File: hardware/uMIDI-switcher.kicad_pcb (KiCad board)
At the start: 2 copper layers, 137.5 x 52.5 mm, 113 parts, among them Q1 BSS138, Q2 BSS138, Q3 BSS138, Q4 BSS138, Q5 BSS138, Q6 BSS138, Q7 BSS138, Q8 BSS138, U1 LM7809CT, U2 LM7809CT, U3 LM7809CT, U4 LM7809CT, X1 CONN_01X02, X10 Jack_Stacked, X11 Jack_Stacked, X14 uMIDI GPIO3, X15 LEDs, X16 uMIDI Power, X2 CONN_01X02, X3 CONN_01X02, X4 CONN_01X02, X5 Jack_Stacked, X6 Jack_Stacked, X7 Jack_Stacked, X8 Jack_Stacked, X9 Jack_Stacked

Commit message: Remove led distribution
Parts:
- removed R1, R2, R3, R4, R5, R6, R7, R8: 630, Resistors_SMD:R_0603
- removed X15: LEDs, Pin_Headers:Pin_Header_Straight_1x10
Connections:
- X14 pad 6: /Loopers and Switches/Looper4 -> (no net)

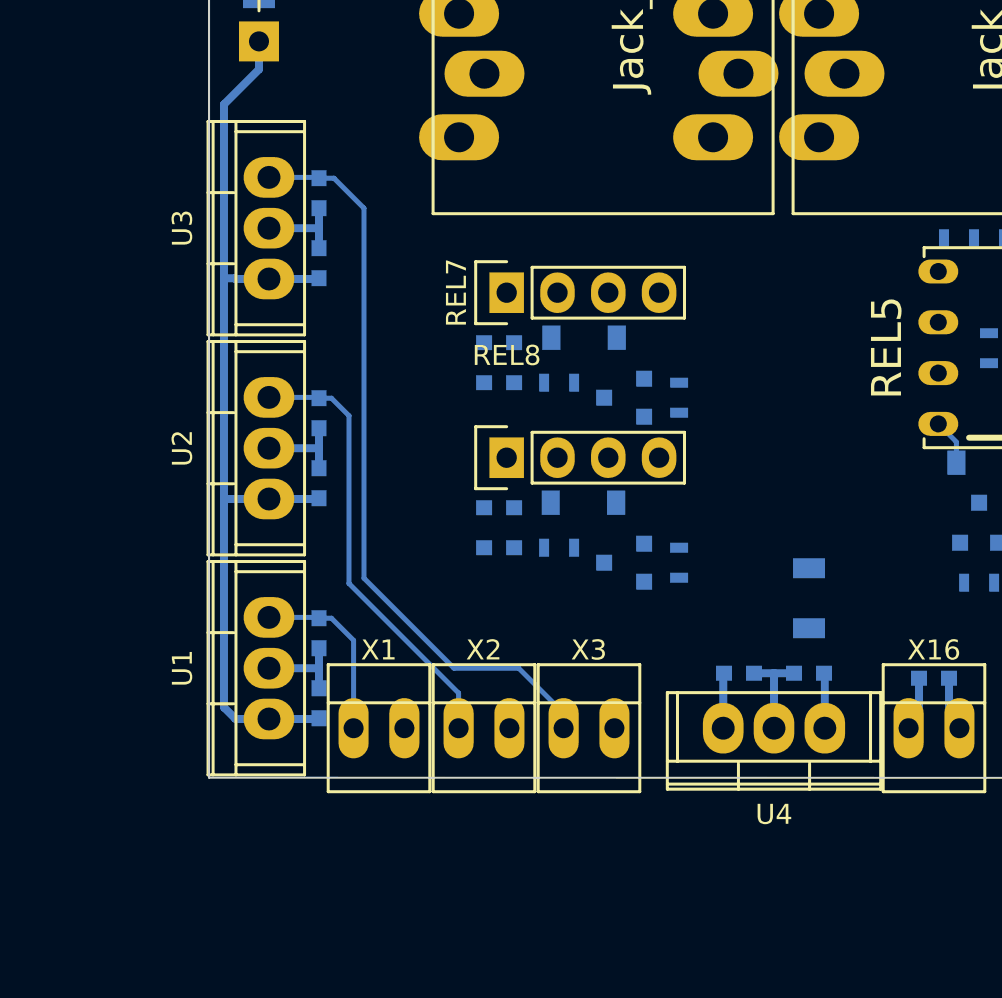
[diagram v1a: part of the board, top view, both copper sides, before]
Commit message: Use smd regulators
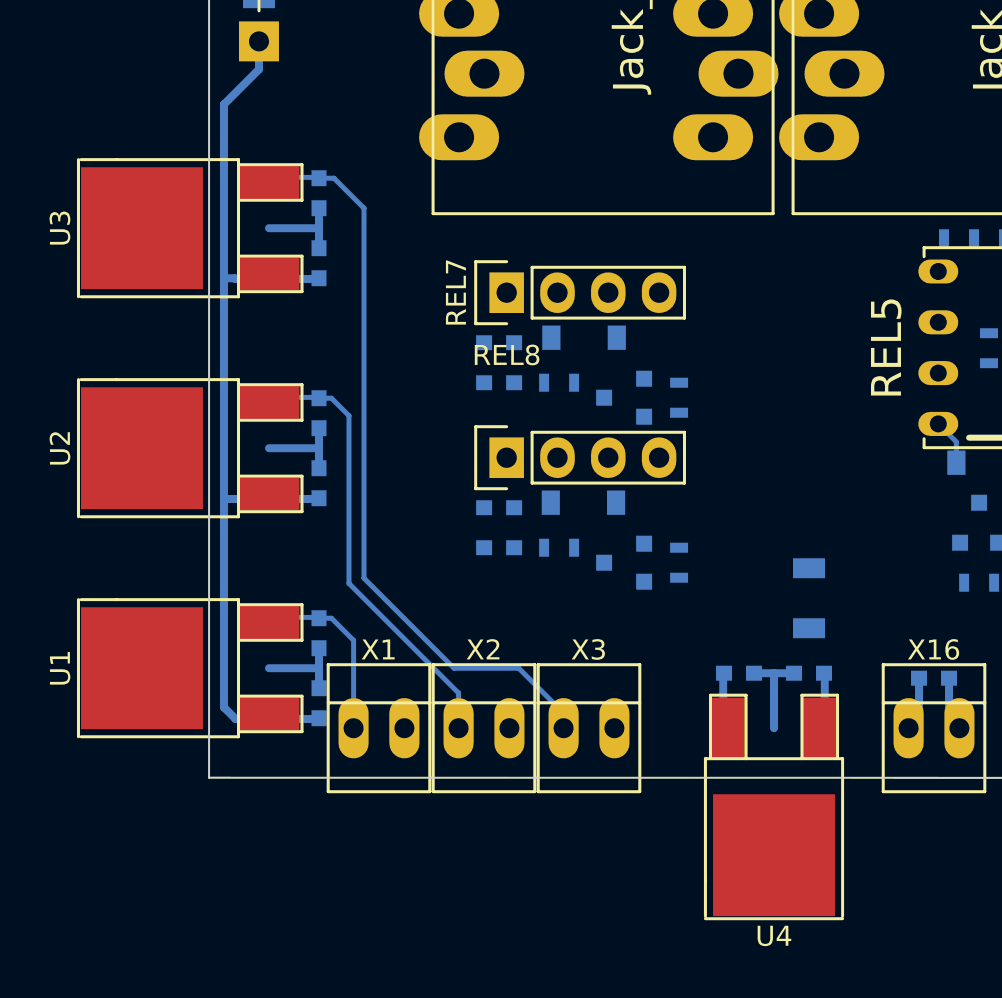
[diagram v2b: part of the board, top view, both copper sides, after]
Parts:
- U1, U2, U3, U4: value LM7809CT -> MC7809CD; footprint Power_Integrations:TO-220 -> TO_SOT_Packages_SMD:TO-252-2Lead

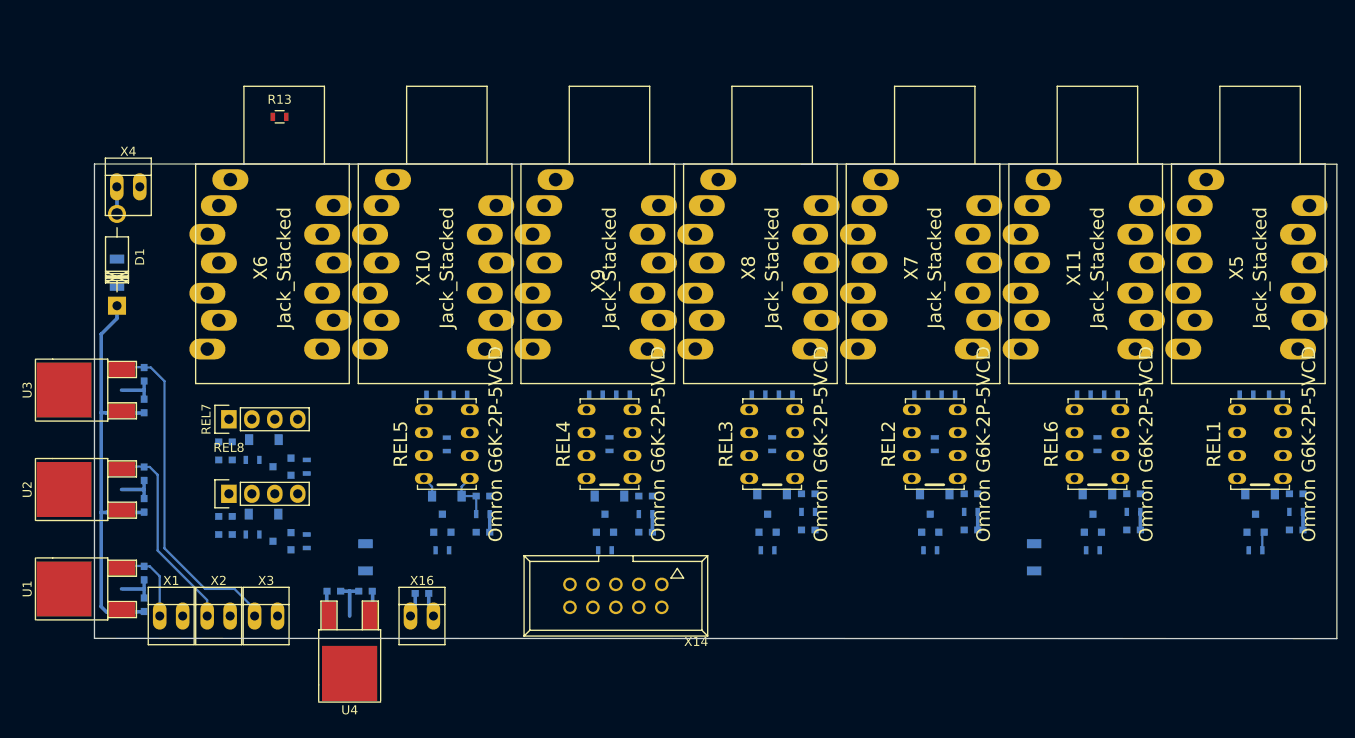
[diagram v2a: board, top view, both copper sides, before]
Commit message: Use schottky diode for input protection
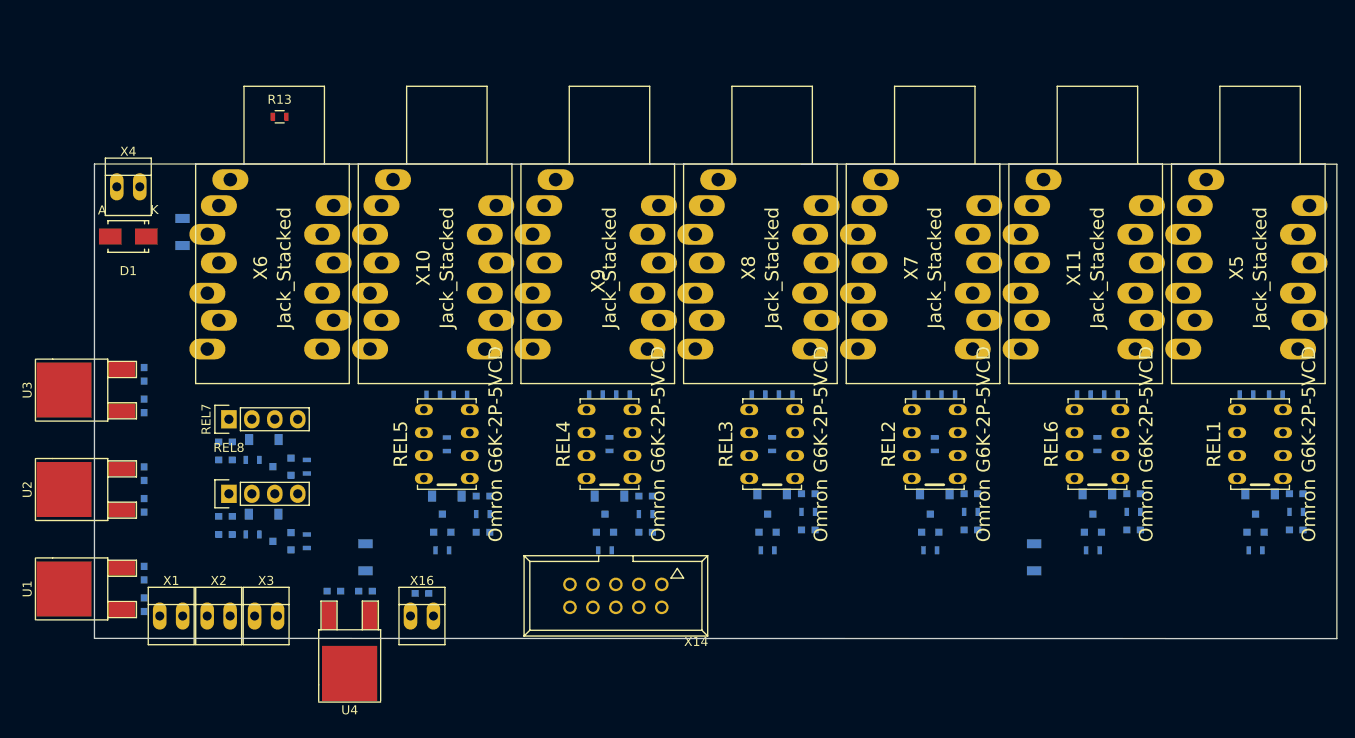
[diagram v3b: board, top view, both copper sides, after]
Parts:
- D1: value 1N4001 -> B160; footprint Diodes_ThroughHole:Diode_DO-41_SOD81_Horizontal_RM10 -> Diodes_SMD:SMA_Standard
- moved C7 8.53 mm to (87.2, 84.0)
- moved D1 7.76 mm to (81.2, 84.5), turned to 180 degrees
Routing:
- net +12V: track 51.3 -> 0.00 mm
- net Net-(C6-Pad1): track 37.4 -> 0.00 mm
- net Net-(C5-Pad1): track 22.3 -> 0.00 mm
- net GND: track 21.0 -> 0.00 mm
- net +9V: track 15.5 -> 0.00 mm
- net Net-(C4-Pad1): track 9.10 -> 0.00 mm
- net /Loopers and Switches/Looper5/Single True Bypass/relais_p: track 5.93 -> 0.00 mm
- net /pwr_in: track 3.01 -> 0.00 mm
- net /Loopers and Switches/Looper5/Single True Bypass/relais_n: track 2.31 -> 0.00 mm
- net /Loopers and Switches/Tune: track 2.09 -> 0.00 mm

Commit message: Straighten annotation and placement
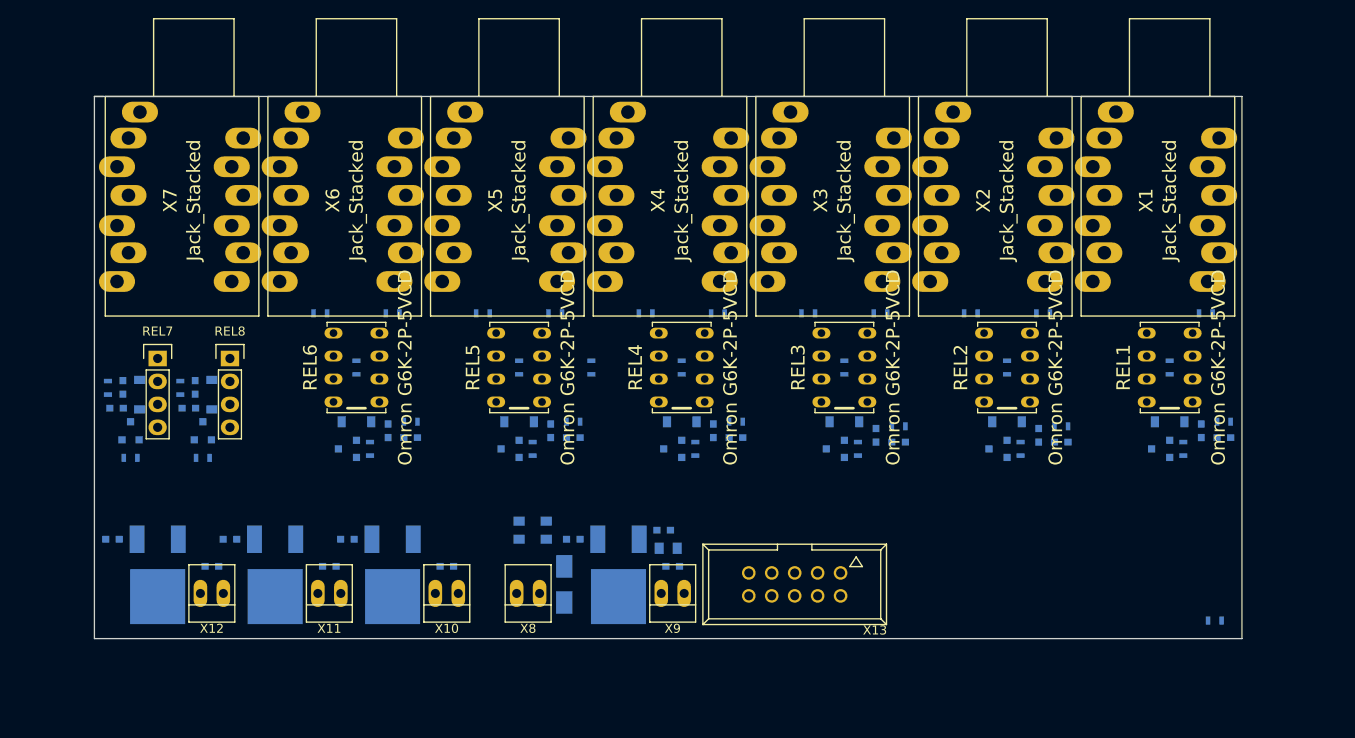
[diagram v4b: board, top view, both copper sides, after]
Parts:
- removed R36, R37, R40, R42, R43: 100M, Resistors_SMD:R_0603
- removed R38, R44, R46, R48: TBD, Resistors_SMD:R_0603
- removed R39, R45, R47, R49: 10k, Resistors_SMD:R_0603
- removed X14: uMIDI GPIO3, Connect:VASCH5x2
- removed X16: uMIDI Power, Connect:PINHEAD1-2
- added R1: 100M, Resistors_SMD:R_0603, B.Cu at (132.5, 99.0)
- added R11: 10k, Resistors_SMD:R_0603, B.Cu at (162.0, 108.0)
- added R17: 100M, Resistors_SMD:R_0603, B.Cu at (128.5, 93.0)
- added R2: 100M, Resistors_SMD:R_0603, B.Cu at (200.5, 93.0)
- added R23: 100M, Resistors_SMD:R_0603, B.Cu at (106.5, 99.0)
- added R29: 100M, Resistors_SMD:R_0603, B.Cu at (174.5, 93.0)
- added R3: 100M, Resistors_SMD:R_0603, B.Cu at (196.5, 99.0)
- added R35: 10k, Resistors_SMD:R_0603, B.Cu at (89.5, 109.0)
- added R4: 100M, Resistors_SMD:R_0603, B.Cu at (201.5, 127.0)
- added R5: 180, Resistors_SMD:R_0603, B.Cu at (202.5, 105.0)
- added R6: 10k, Resistors_SMD:R_0603, B.Cu at (198.0, 108.0)
- added R7: 100M, Resistors_SMD:R_0603, B.Cu at (164.5, 93.0)
- added R8: 100M, Resistors_SMD:R_0603, B.Cu at (160.5, 99.0)
- added R9: 100M, Resistors_SMD:R_0603, B.Cu at (156.5, 93.0)
- added X12: CONN_01X02, Connect:PINHEAD1-2, F.Cu at (90.5, 124.0)
- added X13: uMIDI GPIO, Connect:VASCH5x2, F.Cu at (155.0, 123.0)
- C10: value 10u -> 100n; footprint Capacitors_SMD:C_1206 -> Capacitors_SMD:C_0603
- C11, C7: footprint Capacitors_SMD:C_1206 -> Capacitors_SMD:C_0805
- C8: value 100n -> 10u; footprint Capacitors_SMD:C_0603 -> Capacitors_SMD:C_0805
- D1, R13, U1, U2, U3, U4: moved to B.Cu
- R10, R25, R30, R34: value 100M -> 180
- R14: value TBD -> 100M
- R15: value 10k -> 180
- R16, R31: value 100M -> 10k
- R20, R32: value TBD -> 180
- R26: value TBD -> 10k
- R27: value 10k -> 100M
- X1, X2, X3, X4: value CONN_01X02 -> Jack_Stacked; footprint Connect:PINHEAD1-2 -> uMIDI-switcher:NSJ12HF-1
- X10, X11, X8: value Jack_Stacked -> CONN_01X02; footprint uMIDI-switcher:NSJ12HF-1 -> Connect:PINHEAD1-2
- X9: value Jack_Stacked -> uMIDI Power; footprint uMIDI-switcher:NSJ12HF-1 -> Connect:PINHEAD1-2
- moved X1 124.6 mm to (196.5, 69.0), turned to 90 degrees
- moved X2 104.5 mm to (178.5, 69.0), turned to 90 degrees
- moved X11 97.4 mm to (103.5, 124.0), turned to 180 degrees
- moved C24 90.0 mm to (182.0, 106.5), turned to 270 degrees
- moved X3 86.0 mm to (160.5, 69.0), turned to 90 degrees
- moved C22 83.2 mm to (110.0, 106.0), turned to 270 degrees
- moved REL6 82.4 mm to (106.5, 99.0)
- moved X5 82.3 mm to (124.5, 69.0)
- moved X7 82.3 mm to (88.5, 69.0)
- moved R14 75.3 mm to (138.5, 93.0), turned to 180 degrees
- moved C12 69.1 mm to (141.5, 121.0)
- moved X4 62.1 mm to (142.5, 69.0), turned to 90 degrees
- moved D1 61.7 mm to (129.5, 123.0), turned to 270 degrees
- moved R32 61.1 mm to (79.0, 101.2), turned to 270 degrees
- moved R15 59.2 mm to (148.5, 105.0), turned to 0 degrees
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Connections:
- net /Loopers and Switches/Looper1/Single True Bypass/bypass renamed /Looper5/Single True Bypass/bypass
- net /Loopers and Switches/Looper3/Loop_In renamed /Looper2/Loop_In
- net /Loopers and Switches/Looper4/Loop_In renamed /Looper3/Loop_In
- net /Loopers and Switches/Looper5/Loop_In renamed /Looper4/Loop_In
- net /Loopers and Switches/SwitchRing/relais_n renamed /Switch2/relais_n
- net /Loopers and Switches/SwitchTip/relais_n renamed /Switch1/relais_n
- net /Loopers and Switches/Tuner/relais_n renamed /Tuner/relais_n
- C10 pad 1: +12V -> +9V
- C13 pad 1: /Loopers and Switches/Tuner/relais_p -> +9V
- C14 pad 1: +9V -> /Tuner/relais_p
- C15 pad 1: /Loopers and Switches/Looper2/Single True Bypass/relais_p -> +9V
- C16 pad 1: +9V -> /Looper2/Single True Bypass/relais_p
- C17 pad 1: /Loopers and Switches/Looper3/Single True Bypass/relais_p -> +9V
- C18 pad 1: +9V -> /Looper3/Single True Bypass/relais_p
- C19 pad 1: /Loopers and Switches/Looper4/Single True Bypass/relais_p -> +9V
- C20 pad 1: +9V -> /Looper4/Single True Bypass/relais_p
- C21 pad 1: /Loopers and Switches/Looper5/Single True Bypass/relais_p -> +9V
- C22 pad 1: +9V -> /Looper5/Single True Bypass/relais_p
- C23 pad 1: /Loopers and Switches/Looper1/Single True Bypass/relais_p -> +9V
- C24 pad 1: +9V -> /Looper1/Single True Bypass/relais_p
- C25 pad 1: /Loopers and Switches/SwitchTip/relais_p -> +9V
- C26 pad 1: +9V -> /Switch1/relais_p
- C27 pad 1: /Loopers and Switches/SwitchRing/relais_p -> +9V
- C28 pad 1: +9V -> /Switch2/relais_p
- C9 pad 1: +9V -> +12V
- D2 pad 1: /Loopers and Switches/Tuner/relais_p -> /Tuner/relais_p
- D3 pad 1: /Loopers and Switches/Looper2/Single True Bypass/relais_p -> /Looper2/Single True Bypass/relais_p
- D3 pad 2: /Loopers and Switches/Looper2/Single True Bypass/relais_n -> /Looper2/Single True Bypass/relais_n
- D4 pad 1: /Loopers and Switches/Looper3/Single True Bypass/relais_p -> /Looper3/Single True Bypass/relais_p
- D4 pad 2: /Loopers and Switches/Looper3/Single True Bypass/relais_n -> /Looper3/Single True Bypass/relais_n
- D5 pad 1: /Loopers and Switches/Looper4/Single True Bypass/relais_p -> /Looper4/Single True Bypass/relais_p
- D5 pad 2: /Loopers and Switches/Looper4/Single True Bypass/relais_n -> /Looper4/Single True Bypass/relais_n
- D6 pad 1: /Loopers and Switches/Looper5/Single True Bypass/relais_p -> /Looper5/Single True Bypass/relais_p
- D6 pad 2: /Loopers and Switches/Looper5/Single True Bypass/relais_n -> /Looper5/Single True Bypass/relais_n
- D7 pad 1: /Loopers and Switches/Looper1/Single True Bypass/relais_p -> /Looper1/Single True Bypass/relais_p
- D7 pad 2: /Loopers and Switches/Looper1/Single True Bypass/relais_n -> /Looper1/Single True Bypass/relais_n
- D8 pad 1: /Loopers and Switches/SwitchTip/relais_p -> /Switch1/relais_p
- D9 pad 1: /Loopers and Switches/SwitchRing/relais_p -> /Switch2/relais_p
- Q1 pad 1: /Loopers and Switches/Tune -> /Tuner/Ctrl
- Q2 pad 1: /Loopers and Switches/Looper2 -> /Looper2/Ctrl
- Q2 pad 3: /Loopers and Switches/Looper2/Single True Bypass/relais_n -> /Looper2/Single True Bypass/relais_n
- Q3 pad 1: /Loopers and Switches/Looper3 -> /Looper3/Ctrl
- Q3 pad 3: /Loopers and Switches/Looper3/Single True Bypass/relais_n -> /Looper3/Single True Bypass/relais_n
- Q4 pad 1: /Loopers and Switches/Looper4/Ctrl -> /Looper4/Ctrl
- Q4 pad 3: /Loopers and Switches/Looper4/Single True Bypass/relais_n -> /Looper4/Single True Bypass/relais_n
- Q5 pad 1: /Loopers and Switches/Looper5 -> /Looper5/Ctrl
- Q5 pad 3: /Loopers and Switches/Looper5/Single True Bypass/relais_n -> /Looper5/Single True Bypass/relais_n
- Q6 pad 1: /Loopers and Switches/Looper1 -> /Looper1/Ctrl
- Q6 pad 3: /Loopers and Switches/Looper1/Single True Bypass/relais_n -> /Looper1/Single True Bypass/relais_n
- Q7 pad 1: /Loopers and Switches/SwitchTip -> /Switch1/Ctrl
- Q8 pad 1: /Loopers and Switches/SwitchRing -> /Switch2/Ctrl
- R10 pad 1: /Loopers and Switches/Tuner/FX_Send -> /Looper2/Single True Bypass/relais_p
- R10 pad 2: GNDA -> +9V
- R12 pad 1: /Loopers and Switches/Tuner/bypass -> /Looper3/Single True Bypass/FX_Send
- R13 pad 1: GNDA -> /Looper3/Single True Bypass/bypass
- R14 pad 1: /Loopers and Switches/Tuner/relais_p -> /Looper3/Single True Bypass/FX_Return
- R14 pad 2: +9V -> GNDA
- R15 pad 1: /Loopers and Switches/Tune -> /Looper3/Single True Bypass/relais_p
- R15 pad 2: GND -> +9V
- R16 pad 1: /Loopers and Switches/Looper2/Single True Bypass/FX_Send -> /Looper3/Ctrl
- R16 pad 2: GNDA -> GND
- R18 pad 1: /Loopers and Switches/Looper2/Single True Bypass/bypass -> /Looper4/Single True Bypass/bypass
- R19 pad 1: /Loopers and Switches/Looper2/Single True Bypass/FX_Return -> /Looper4/Single True Bypass/FX_Return
- R20 pad 1: /Loopers and Switches/Looper2/Single True Bypass/relais_p -> /Looper4/Single True Bypass/relais_p
- R21 pad 1: /Loopers and Switches/Looper2 -> /Looper4/Ctrl
- R22 pad 1: /Loopers and Switches/Looper3/Single True Bypass/FX_Send -> /Looper5/Single True Bypass/FX_Send
- R24 pad 1: /Loopers and Switches/Looper3/Single True Bypass/bypass -> /Looper5/Single True Bypass/FX_Return
- R25 pad 1: /Loopers and Switches/Looper3/Single True Bypass/FX_Return -> /Looper5/Single True Bypass/relais_p
- R25 pad 2: GNDA -> +9V
- R26 pad 1: /Loopers and Switches/Looper3/Single True Bypass/relais_p -> /Looper5/Ctrl
- R26 pad 2: +9V -> GND
- R27 pad 1: /Loopers and Switches/Looper3 -> /Looper1/Single True Bypass/FX_Send
- R27 pad 2: GND -> GNDA
- R28 pad 1: /Loopers and Switches/Looper4/Single True Bypass/FX_Send -> /Looper1/Single True Bypass/bypass
- R30 pad 1: /Loopers and Switches/Looper4/Single True Bypass/bypass -> /Looper1/Single True Bypass/relais_p
- R30 pad 2: GNDA -> +9V
- R31 pad 1: /Loopers and Switches/Looper4/Single True Bypass/FX_Return -> /Looper1/Ctrl
- R31 pad 2: GNDA -> GND
- R32 pad 1: /Loopers and Switches/Looper4/Single True Bypass/relais_p -> /Switch1/relais_p
- R33 pad 1: /Loopers and Switches/Looper4/Ctrl -> /Switch1/Ctrl
- R34 pad 1: /Loopers and Switches/Looper5/Single True Bypass/FX_Send -> /Switch2/relais_p
- R34 pad 2: GNDA -> +9V
- REL1 pad 1: /Loopers and Switches/Tuner/relais_p -> /Tuner/relais_p
- REL1 pad 2: /Loopers and Switches/Tuner/bypass -> /Tuner/bypass
- REL1 pad 3: /Loopers and Switches/Tuner/Loop_In -> /Tuner/Loop_In
- REL1 pad 4: /Loopers and Switches/Tuner/FX_Send -> /Tuner/FX_Send
- REL1 pad 6: /Loopers and Switches/Looper1/Loop_In -> /Looper1/Loop_In
- REL1 pad 7: /Loopers and Switches/Tuner/bypass -> /Tuner/bypass
- REL2 pad 1: /Loopers and Switches/Looper2/Single True Bypass/relais_p -> /Looper1/Single True Bypass/relais_p
- REL2 pad 2: /Loopers and Switches/Looper2/Single True Bypass/bypass -> /Looper1/Single True Bypass/bypass
- REL2 pad 3: /Loopers and Switches/Looper2/Loop_In -> /Looper1/Loop_In
- REL2 pad 4: /Loopers and Switches/Looper2/Single True Bypass/FX_Send -> /Looper1/Single True Bypass/FX_Send
- REL2 pad 5: /Loopers and Switches/Looper2/Single True Bypass/FX_Return -> /Looper1/Single True Bypass/FX_Return
- REL2 pad 7: /Loopers and Switches/Looper2/Single True Bypass/bypass -> /Looper1/Single True Bypass/bypass
- REL2 pad 8: /Loopers and Switches/Looper2/Single True Bypass/relais_n -> /Looper1/Single True Bypass/relais_n
- REL3 pad 1: /Loopers and Switches/Looper3/Single True Bypass/relais_p -> /Looper2/Single True Bypass/relais_p
- REL3 pad 2: /Loopers and Switches/Looper3/Single True Bypass/bypass -> /Looper2/Single True Bypass/bypass
- REL3 pad 4: /Loopers and Switches/Looper3/Single True Bypass/FX_Send -> /Looper2/Single True Bypass/FX_Send
- REL3 pad 5: /Loopers and Switches/Looper3/Single True Bypass/FX_Return -> /Looper2/Single True Bypass/FX_Return
- REL3 pad 7: /Loopers and Switches/Looper3/Single True Bypass/bypass -> /Looper2/Single True Bypass/bypass
- REL3 pad 8: /Loopers and Switches/Looper3/Single True Bypass/relais_n -> /Looper2/Single True Bypass/relais_n
- REL4 pad 1: /Loopers and Switches/Looper4/Single True Bypass/relais_p -> /Looper3/Single True Bypass/relais_p
- REL4 pad 2: /Loopers and Switches/Looper4/Single True Bypass/bypass -> /Looper3/Single True Bypass/bypass
- REL4 pad 4: /Loopers and Switches/Looper4/Single True Bypass/FX_Send -> /Looper3/Single True Bypass/FX_Send
- REL4 pad 5: /Loopers and Switches/Looper4/Single True Bypass/FX_Return -> /Looper3/Single True Bypass/FX_Return
- REL4 pad 7: /Loopers and Switches/Looper4/Single True Bypass/bypass -> /Looper3/Single True Bypass/bypass
- REL4 pad 8: /Loopers and Switches/Looper4/Single True Bypass/relais_n -> /Looper3/Single True Bypass/relais_n
- REL5 pad 1: /Loopers and Switches/Looper5/Single True Bypass/relais_p -> /Looper4/Single True Bypass/relais_p
- REL5 pad 2: /Loopers and Switches/Looper5/Single True Bypass/bypass -> /Looper4/Single True Bypass/bypass
- REL5 pad 4: /Loopers and Switches/Looper5/Single True Bypass/FX_Send -> /Looper4/Single True Bypass/FX_Send
- REL5 pad 5: /Loopers and Switches/Looper5/Single True Bypass/FX_Return -> /Looper4/Single True Bypass/FX_Return
- REL5 pad 6: /Loopers and Switches/Looper5/Loop_Out -> /Looper5/Loop_In
- REL5 pad 7: /Loopers and Switches/Looper5/Single True Bypass/bypass -> /Looper4/Single True Bypass/bypass
- REL5 pad 8: /Loopers and Switches/Looper5/Single True Bypass/relais_n -> /Looper4/Single True Bypass/relais_n
- REL6 pad 1: /Loopers and Switches/Looper1/Single True Bypass/relais_p -> /Looper5/Single True Bypass/relais_p
- REL6 pad 3: /Loopers and Switches/Looper1/Loop_In -> /Looper5/Loop_In
- REL6 pad 4: /Loopers and Switches/Looper1/Single True Bypass/FX_Send -> /Looper5/Single True Bypass/FX_Send
- REL6 pad 5: /Loopers and Switches/Looper1/Single True Bypass/FX_Return -> /Looper5/Single True Bypass/FX_Return
- REL6 pad 6: /Loopers and Switches/Looper2/Loop_In -> /Looper5/Loop_Out
- REL6 pad 8: /Loopers and Switches/Looper1/Single True Bypass/relais_n -> /Looper5/Single True Bypass/relais_n
- REL7 pad 1: /Loopers and Switches/SwitchTip/A -> /Switch1/A
- REL7 pad 2: /Loopers and Switches/SwitchTip/relais_p -> /Switch1/relais_p
- REL7 pad 4: /Loopers and Switches/SwitchRing/B -> /Switch1/B
- REL8 pad 1: /Loopers and Switches/SwitchRing/A -> /Switch2/A
- REL8 pad 2: /Loopers and Switches/SwitchRing/relais_p -> /Switch2/relais_p
- REL8 pad 4: /Loopers and Switches/SwitchRing/B -> /Switch1/B
- X1 pad 1: Net-(C4-Pad1) -> GNDA
- X1 pad 2: GND -> GNDA
- X10 pad 1: GNDA -> Net-(C4-Pad1)
- X10 pad 2: GNDA -> GND
- X11 pad 1: GNDA -> Net-(C5-Pad1)
- X11 pad 2: GNDA -> GND
- X2 pad 1: Net-(C5-Pad1) -> GNDA
- X2 pad 2: GND -> GNDA
- X3 pad 1: Net-(C6-Pad1) -> GNDA
- X3 pad 2: GND -> GNDA
- X4 pad 1: /pwr_in -> GNDA
- X4 pad 2: GND -> GNDA
- X5 pad 3: GNDA -> /Looper4/Single True Bypass/FX_Send
- X5 pad 6: /Loopers and Switches/Tuner/Loop_In -> /Looper4/Single True Bypass/FX_Return
- X5 pad 7: /Loopers and Switches/Tuner/FX_Send -> GNDA
- X5 pad 8: (no net) -> GNDA
- X6 pad 11: (no net) -> GNDA
- X6 pad 13: (no net) -> GNDA
- X6 pad 2: /Loopers and Switches/SwitchRing/B -> GNDA
- X6 pad 3: GNDA -> /Looper5/Single True Bypass/FX_Send
- X6 pad 4: /Loopers and Switches/SwitchRing/A -> GNDA
- X6 pad 6: /Loopers and Switches/SwitchTip/A -> /Looper5/Single True Bypass/FX_Return
- X6 pad 7: /Loopers and Switches/Looper5/Loop_Out -> GNDA
- X6 pad 8: (no net) -> GNDA
- X7 pad 11: GNDA -> (no net)
- X7 pad 13: GNDA -> (no net)
- X7 pad 2: GNDA -> /Switch1/B
- X7 pad 3: /Loopers and Switches/Looper2/Single True Bypass/FX_Send -> GNDA
- X7 pad 4: GNDA -> /Switch2/A
- X7 pad 6: /Loopers and Switches/Looper2/Single True Bypass/FX_Return -> /Switch1/A
- X7 pad 7: GNDA -> /Looper5/Loop_Out
- X7 pad 8: GNDA -> (no net)
- X8 pad 1: GNDA -> /pwr_in
- X8 pad 2: GNDA -> GND
- X9 pad 1: GNDA -> +9V
- X9 pad 2: GNDA -> GND
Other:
- board size 137.5 x 52.5 mm -> 127 x 60 mm

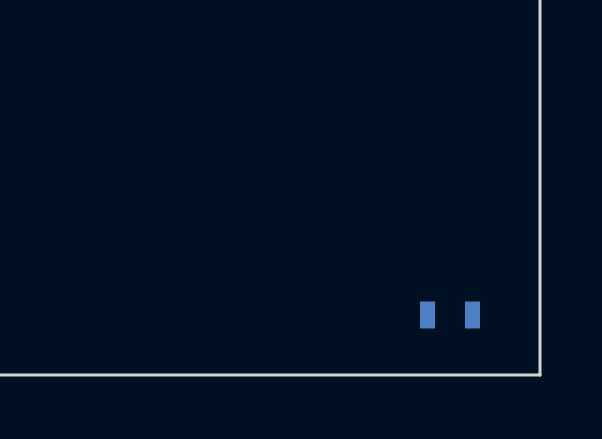
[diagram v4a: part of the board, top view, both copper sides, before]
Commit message: Remove tuner signal to GNDA resistor (only on board)
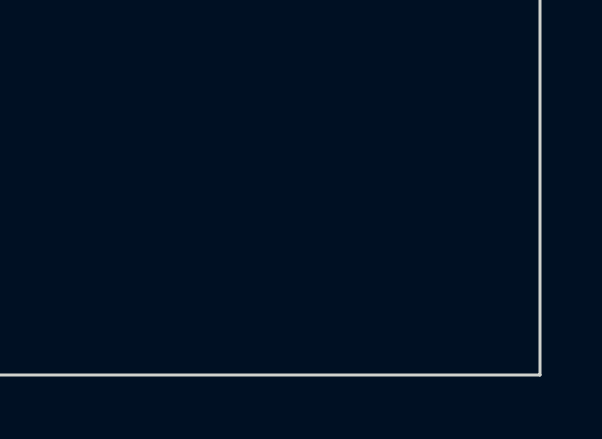
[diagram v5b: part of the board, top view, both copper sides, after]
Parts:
- removed R4: 100M, Resistors_SMD:R_0603
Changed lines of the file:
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@@
     (tracks 0)
     (zones 0)
-    (modules 105)
+    (modules 104)
     (nets 60)
   )
@@
       (net 7 GNDA))
     (model Resistors_SMD.3dshapes/R_0603.wrl
-      (at (xyz 0 0 0))
-      (scale (xyz 1 1 1))
-      (rotate (xyz 0 0 0))
-    )
-  )
-  (module Resistors_SMD:R_0603 (layer B.Cu)
-    (at 201.5 127)
-    (descr "Resistor SMD 0603, reflow soldering, Vishay (see dcrcw.pdf)")
-    (tags "resistor 0603")
-    (attr smd)
-    (fp_text reference R4 (at 0 1.9) (layer B.SilkS)
-      (effects (font (size 1 1) (thickness 0.15)) (justify mirror))
-    )
-    (fp_text value 100M (at 0 -1.9) (layer B.Fab)
-      (effects (font (size 1 1) (thickness 0.15)) (justify mirror))
-    )
-    (fp_line (start -1.3 0.8) (end 1.3 0.8) (layer B.CrtYd) (width 0.05))
-    (fp_line (start -1.3 -0.8) (end 1.3 -0.8) (layer B.CrtYd) (width 0.05))
-    (fp_line (start -1.3 0.8) (end -1.3 -0.8) (layer B.CrtYd) (width 0.05))
-    (fp_line (start 1.3 0.8) (end 1.3 -0.8) (layer B.CrtYd) (width 0.05))
-    (fp_line (start 0.5 -0.675) (end -0.5 -0.675) (layer B.SilkS) (width 0.15))
-    (fp_line (start -0.5 0.675) (end 0.5 0.675) (layer B.SilkS) (width 0.15))
-    (pad 1 smd rect (at -0.75 0) (size 0.5 0.9) (layers B.Cu B.Paste B.Mask)
-      (net 7 GNDA))
-    (pad 2 smd rect (at 0.75 0) (size 0.5 0.9) (layers B.Cu B.Paste B.Mask)
-      (net 7 GNDA))
-    (model Resistors_SMD.3dshapes/R_0603.wrl
